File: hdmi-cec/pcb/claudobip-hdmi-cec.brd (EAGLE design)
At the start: 43.9 x 51 mm, 26 parts, among them IC1 LD117AV33, Q1 16mhz, SW1 PUSH_BUTTON_SWITCH, T1 2N3904, T2 2N3904, U1 ATMEGA328P-AU, X2 MINI-USB_5P

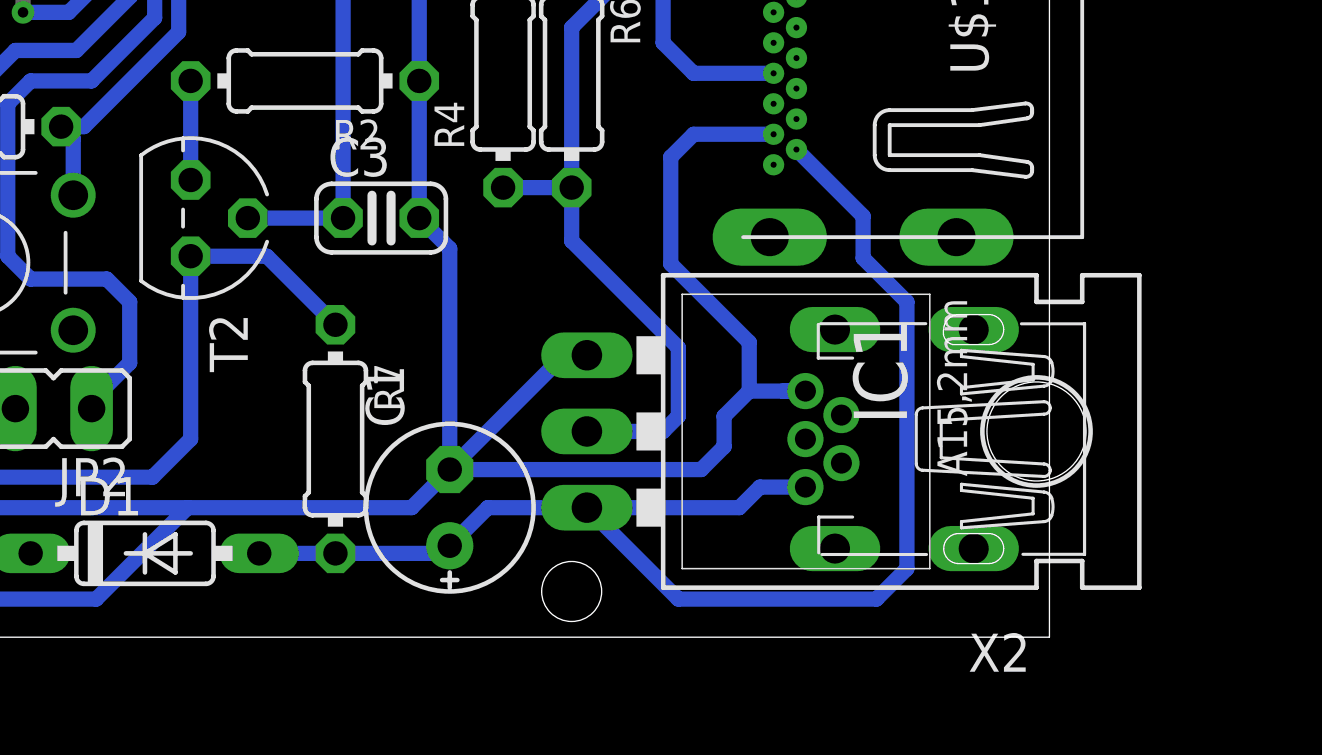
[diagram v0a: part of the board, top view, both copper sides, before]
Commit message: [HDMI-CEC] Use a vertical footprint for the LD117AV33 regulator
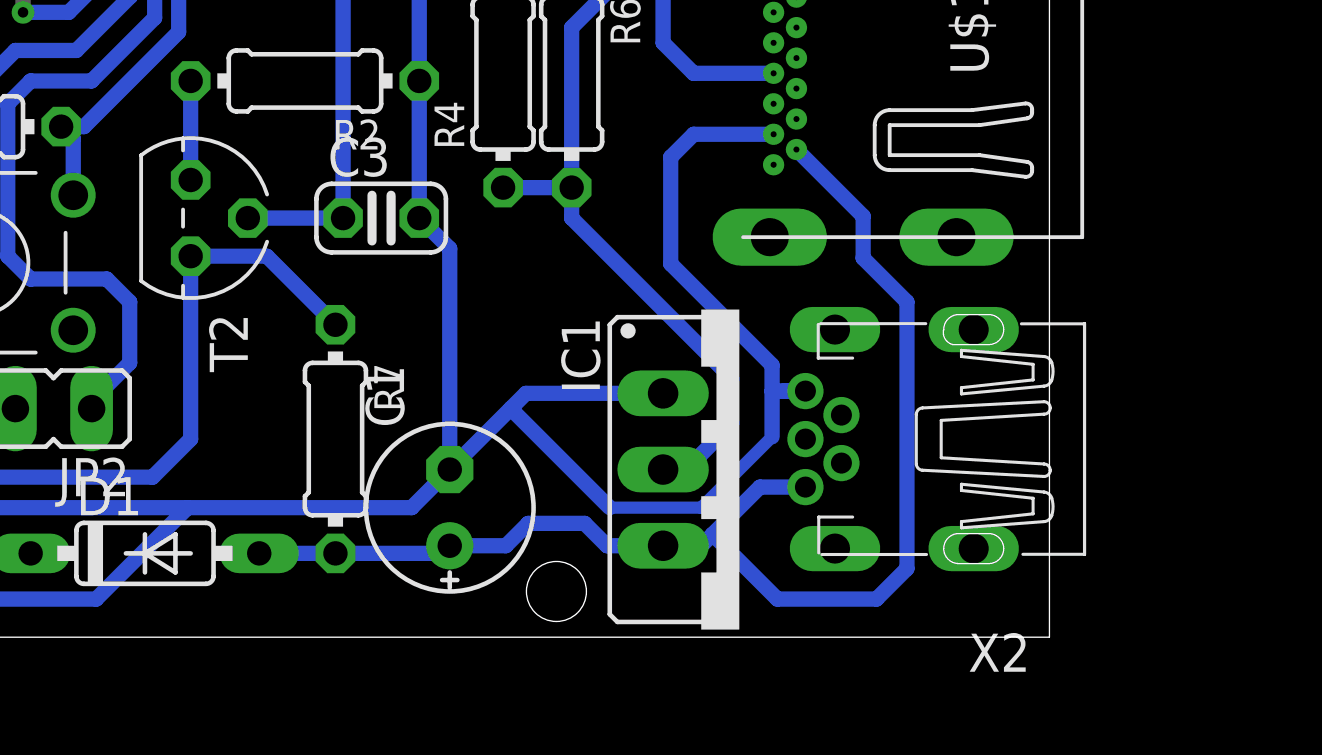
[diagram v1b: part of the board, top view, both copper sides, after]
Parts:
- IC1: value LD117AV33 -> LD117AV33-VERTICAL; device v-reg:TO220L1 -> regulator:TO220S-VERTICAL
- moved IC1 1.80 mm to (33.5, 5.59)
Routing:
- net VCC: track 46.6 -> 42.7 mm
- net GND: track 179.6 -> 182.1 mm
- net +3V3: track 60.6 -> 61.3 mm
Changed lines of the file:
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@@
 <text x="35.56" y="30.226" size="1.4224" layer="16" rot="MR90">@hiteule - May 2022</text>
 <hole x="1.524" y="49.53" drill="2"/>
-<hole x="27.94" y="1.524" drill="2"/>
+<hole x="27.432" y="1.524" drill="2"/>
 <hole x="1.524" y="1.524" drill="2"/>
 <hole x="42.418" y="49.53" drill="2"/>
@@
 <attribute name="VALUE" x="25.273" y="34.798" size="1.27" layer="27" ratio="10" rot="R270"/>
 </element>
-<element name="IC1" library="v-reg" library_urn="urn:adsk.eagle:library:409" package="TO220L1" package3d_urn="urn:adsk.eagle:package:30365/1" value="LD117AV33" x="32.258" y="6.858" smashed="yes" rot="R270">
-<attribute name="NAME" x="37.338" y="10.668" size="1.778" layer="25" ratio="10" rot="R270"/>
-<attribute name="POPULARITY" value="0" x="25.908" y="-16.002" size="1.778" layer="27" rot="R270" display="off"/>
-<attribute name="VALUE" x="34.798" y="10.795" size="1.778" layer="27" ratio="10" rot="R270"/>
-</element>
 <element name="JP1" library="jumper" library_urn="urn:adsk.eagle:library:252" package="JP1" package3d_urn="urn:adsk.eagle:package:15455/1" value="GND/VCC" x="4.318" y="7.62" smashed="yes" rot="R90">
 <attribute name="NAME" x="6.858" y="5.969" size="1.27" layer="25" ratio="10" rot="R180"/>
@@
 <attribute name="NAME" x="43.2315" y="0.1181" size="1.27" layer="25" rot="R180"/>
 <attribute name="VALUE" x="43.5139" y="14.4567" size="1.27" layer="27" rot="R180"/>
+</element>
+<element name="IC1" library="regulator" package="TO220S-VERTICAL" value="LD117AV33-VERTICAL" x="33.528" y="5.588" smashed="yes" rot="R270">
+<attribute name="NAME" x="27.6098" y="10.668" size="1.27" layer="25" ratio="10" rot="R270"/>
+<attribute name="VALUE" x="25.908" y="10.668" size="1.27" layer="27" ratio="10" rot="R270"/>
 </element>
 </elements>
@@
 <contactref element="SW1" pad="3"/>
 <contactref element="JP1" pad="1"/>
-<contactref element="IC1" pad="1"/>
-<contactref element="C1" pad="-"/>
 <contactref element="R1" pad="1"/>
 <contactref element="R2" pad="1"/>
@@
 <wire x1="4.826" y1="10.232" x2="5.588" y2="9.47" width="0.508" layer="16"/>
 <wire x1="5.588" y1="9.47" x2="5.588" y2="7.62" width="0.508" layer="16"/>
-<wire x1="23.876" y1="5.588" x2="27.686" y2="9.398" width="0.508" layer="16"/>
-<wire x1="28.448" y1="9.398" x2="27.686" y2="9.398" width="0.508" layer="16"/>
-<wire x1="23.876" y1="5.588" x2="23.876" y2="12.954" width="0.508" layer="16"/>
-<wire x1="23.876" y1="12.954" x2="22.86" y2="13.97" width="0.508" layer="16"/>
+<wire x1="22.86" y1="13.97" x2="23.876" y2="12.954" width="0.508" layer="16"/>
 <wire x1="22.86" y1="18.542" x2="22.86" y2="13.97" width="0.508" layer="16"/>
 <wire x1="22.86" y1="23.114" x2="22.86" y2="18.542" width="0.508" layer="16"/>
 <wire x1="21.082" y1="35.814" x2="23.368" y2="35.814" width="0.508" layer="16"/>
-<wire x1="22.606" y1="4.318" x2="23.876" y2="5.588" width="0.508" layer="16"/>
-<wire x1="22.606" y1="4.318" x2="15.1384" y2="4.318" width="0.508" layer="16"/>
+<wire x1="15.1384" y1="4.318" x2="22.606" y2="4.318" width="0.508" layer="16"/>
 <wire x1="3.048" y1="28.702" x2="3.048" y2="28.448" width="0.508" layer="16"/>
 <wire x1="3.048" y1="28.448" x2="1.27" y2="26.67" width="0.508" layer="16"/>
@@
 <contactref element="X2" pad="5"/>
 <wire x1="35.7322" y1="8.204" x2="34.976" y2="8.204" width="0.508" layer="16"/>
-<wire x1="35.7322" y1="8.204" x2="33.858" y2="8.204" width="0.508" layer="16"/>
-<wire x1="33.858" y1="8.204" x2="33.02" y2="7.366" width="0.508" layer="16"/>
-<wire x1="33.02" y1="7.366" x2="33.02" y2="6.35" width="0.508" layer="16"/>
-<wire x1="33.02" y1="6.35" x2="32.258" y2="5.588" width="0.508" layer="16"/>
-<wire x1="32.258" y1="5.588" x2="23.876" y2="5.588" width="0.508" layer="16"/>
+<wire x1="35.7322" y1="8.204" x2="34.62" y2="8.204" width="0.508" layer="16"/>
 <wire x1="32.004" y1="16.764" x2="31.242" y2="16.002" width="0.508" layer="16"/>
 <wire x1="32.004" y1="16.764" x2="34.671" y2="16.764" width="0.508" layer="16"/>
@@
 <wire x1="14.586" y1="25.978" x2="15.386" y2="26.778" width="0.508" layer="16"/>
 <wire x1="31.242" y1="16.002" x2="31.242" y2="12.446" width="0.508" layer="16"/>
-<wire x1="33.858" y1="9.83" x2="33.858" y2="8.204" width="0.508" layer="16"/>
-<wire x1="31.242" y1="12.446" x2="33.858" y2="9.83" width="0.508" layer="16"/>
+<wire x1="34.62" y1="9.068" x2="34.62" y2="8.204" width="0.508" layer="16"/>
+<wire x1="31.242" y1="12.446" x2="34.62" y2="9.068" width="0.508" layer="16"/>
 <wire x1="5.588" y1="7.62" x2="5.588" y2="5.334" width="0.508" layer="16"/>
 <wire x1="5.588" y1="5.334" x2="6.604" y2="4.318" width="0.508" layer="16"/>
 <wire x1="6.604" y1="4.318" x2="15.1384" y2="4.318" width="0.508" layer="16"/>
+<contactref element="IC1" pad="1"/>
+<contactref element="C1" pad="-"/>
+<wire x1="22.606" y1="4.318" x2="23.876" y2="5.588" width="0.508" layer="16"/>
+<wire x1="23.876" y1="5.588" x2="25.908" y2="7.62" width="0.508" layer="16"/>
+<wire x1="25.908" y1="7.62" x2="26.416" y2="8.128" width="0.508" layer="16"/>
+<wire x1="26.416" y1="8.128" x2="30.988" y2="8.128" width="0.508" layer="16"/>
+<wire x1="34.62" y1="6.68" x2="34.62" y2="8.204" width="0.508" layer="16"/>
+<wire x1="25.908" y1="7.62" x2="29.21" y2="4.318" width="0.508" layer="16"/>
+<wire x1="23.876" y1="12.954" x2="23.876" y2="5.588" width="0.508" layer="16"/>
+<wire x1="29.21" y1="4.318" x2="32.258" y2="4.318" width="0.4064" layer="16"/>
+<wire x1="32.258" y1="4.318" x2="34.62" y2="6.68" width="0.4064" layer="16"/>
 </signal>
 <signal name="N$5">
@@
 <wire x1="39.116" y1="11.176" x2="39.116" y2="2.286" width="0.508" layer="16"/>
 <wire x1="39.116" y1="2.286" x2="38.1" y2="1.27" width="0.508" layer="16"/>
-<wire x1="31.496" y1="1.27" x2="38.1" y2="1.27" width="0.508" layer="16"/>
-<wire x1="35.7322" y1="5.004" x2="34.214" y2="5.004" width="0.508" layer="16"/>
-<wire x1="34.214" y1="5.004" x2="33.528" y2="4.318" width="0.508" layer="16"/>
+<wire x1="34.214" y1="5.004" x2="35.7322" y2="5.004" width="0.508" layer="16"/>
+<contactref element="C1" pad="+"/>
 <contactref element="IC1" pad="3"/>
-<contactref element="C1" pad="+"/>
-<wire x1="23.876" y1="3.048" x2="25.146" y2="4.318" width="0.508" layer="16"/>
-<wire x1="28.448" y1="4.318" x2="25.146" y2="4.318" width="0.508" layer="16"/>
-<wire x1="28.448" y1="4.318" x2="31.496" y2="1.27" width="0.508" layer="16"/>
-<wire x1="33.528" y1="4.318" x2="28.448" y2="4.318" width="0.508" layer="16"/>
+<wire x1="38.1" y1="1.27" x2="34.798" y2="1.27" width="0.508" layer="16"/>
+<wire x1="30.988" y1="3.048" x2="32.258" y2="3.048" width="0.508" layer="16"/>
+<wire x1="32.258" y1="3.048" x2="32.639" y2="3.429" width="0.508" layer="16"/>
+<wire x1="32.639" y1="3.429" x2="34.214" y2="5.004" width="0.508" layer="16"/>
+<wire x1="34.798" y1="1.27" x2="32.639" y2="3.429" width="0.508" layer="16"/>
+<wire x1="23.876" y1="3.048" x2="25.74573125" y2="3.048" width="0.508" layer="16"/>
+<wire x1="25.74573125" y1="3.048" x2="26.49173125" y2="3.794" width="0.508" layer="16"/>
+<wire x1="26.49173125" y1="3.794" x2="28.37226875" y2="3.794" width="0.508" layer="16"/>
+<wire x1="28.37226875" y1="3.794" x2="29.11826875" y2="3.048" width="0.508" layer="16"/>
+<wire x1="29.11826875" y1="3.048" x2="30.988" y2="3.048" width="0.508" layer="16"/>
 <wire x1="23.622" y1="2.794" x2="23.876" y2="3.048" width="0" layer="19" extent="16-16"/>
 </signal>
@@
 </signal>
 <signal name="+3V3">
-<contactref element="IC1" pad="2"/>
 <contactref element="R4" pad="1"/>
 <contactref element="R6" pad="2"/>
@@
 <wire x1="29.718" y1="31.242" x2="13.716" y2="47.244" width="0.508" layer="16"/>
 <wire x1="13.716" y1="47.244" x2="7.366" y2="47.244" width="0.508" layer="16"/>
-<wire x1="28.448" y1="6.858" x2="30.988" y2="6.858" width="0.508" layer="16"/>
-<wire x1="30.988" y1="6.858" x2="31.496" y2="7.366" width="0.508" layer="16"/>
-<wire x1="31.496" y1="7.366" x2="31.496" y2="9.652" width="0.508" layer="16"/>
-<wire x1="31.496" y1="9.652" x2="27.94" y2="13.208" width="0.508" layer="16"/>
-<wire x1="27.94" y1="13.208" x2="27.94" y2="14.986" width="0.508" layer="16"/>
 <wire x1="25.654" y1="14.986" x2="27.94" y2="14.986" width="0.508" layer="16"/>
+<contactref element="IC1" pad="2"/>
+<wire x1="27.94" y1="14.986" x2="27.94" y2="13.97" width="0.508" layer="16"/>
+<wire x1="27.94" y1="13.97" x2="33.274" y2="8.636" width="0.508" layer="16"/>
+<wire x1="33.274" y1="8.636" x2="33.274" y2="7.112" width="0.508" layer="16"/>
+<wire x1="33.274" y1="7.112" x2="31.75" y2="5.588" width="0.508" layer="16"/>
+<wire x1="31.75" y1="5.588" x2="30.988" y2="5.588" width="0.508" layer="16"/>
 </signal>
 <signal name="N$12">
